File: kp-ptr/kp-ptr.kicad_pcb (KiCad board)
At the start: 2 copper layers, 125 parts, among them IC1 E22-900M22S, J2 Conn_01x02, J3 Conn_01x02, J4 USB_C_Receptacle_USB2.0, J6 Conn_01x02, J7 Conn_01x02, J8 Conn_01x02, J9 Conn_01x02, Q10 NMOS_SOT23, Q11 NMOS_SOT23, Q12 PMOS_SOT23, Q13 PMOS_SOT23, Q5 NMOS_SOT23, Q6 NMOS_SOT23, Q7 NMOS_SOT23, Q8 PMOS_SOT23, Q9 PMOS_SOT23, U1 ESP32-S3FN8, U10 USBLC6-2SC6, U3 MS560702BA03-50, U4 MMC5983MA, U5 H3LIS331, U6 L96-M33, U7 LSM6DSO32, U8 SPX3819M5-L-3-3, U9 SPX3819M5-L-1-8, Y1 7M40000005-40MHz

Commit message: Small changes before sleep Signed-off-by: kretu <krecik@gmail.com>
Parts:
- added J5: Micro_SD_Card_Det, KP-PTR_lib:GCT_MEM2051-00-195-00-A, F.Cu at (222.1, 34.6)
- moved R26 101.0 mm to (152.5, 80.0), turned to -90 degrees
- moved C33 90.5 mm to (166.3, 73.9), turned to 180 degrees
- moved C31 89.4 mm to (168.2, 70.5)
- moved R25 83.0 mm to (168.4, 73.4)
- moved R27 82.7 mm to (168.4, 71.3)
- moved C32 82.6 mm to (166.3, 73.3), turned to 180 degrees
- moved R24 79.8 mm to (167.2, 72.4)
- moved R36 44.2 mm to (213.4, 38.3), turned to 180 degrees
- moved R31 40.1 mm to (221.3, 43.7)
- moved R33 31.8 mm to (222.4, 45.7), turned to 180 degrees
- moved R32 31.5 mm to (224.7, 43.7)
- moved R28 17.6 mm to (258.5, 101.3)
- moved C36 14.4 mm to (259.5, 102.6)
- moved R39 10.1 mm to (271.4, 73.8)
- moved U8 5.60 mm to (162.6, 71.4), turned to 180 degrees
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
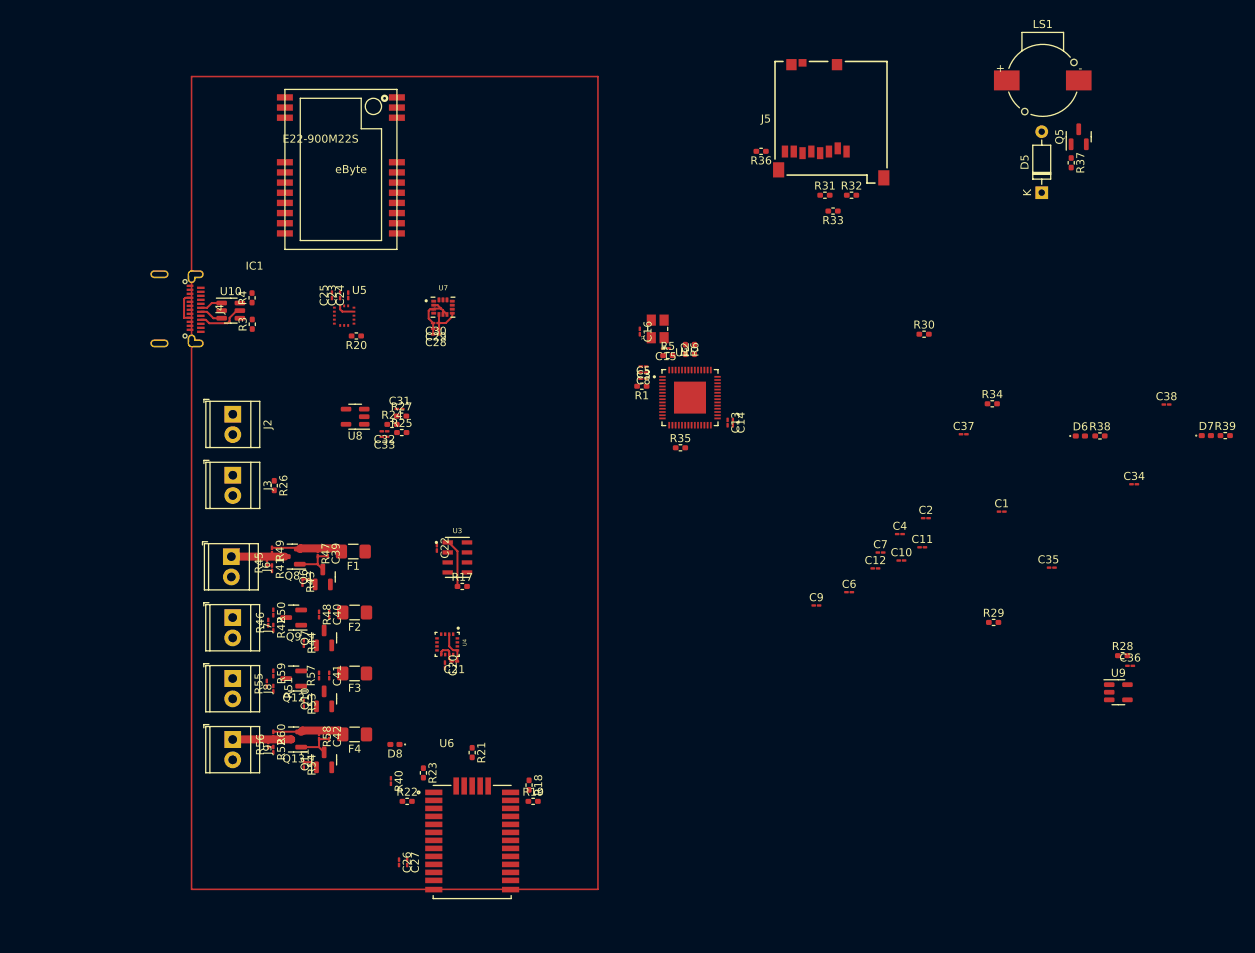
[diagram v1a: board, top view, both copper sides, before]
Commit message: Golaiath fight with board Signed-off-by: kretu <krecik@gmail.com>
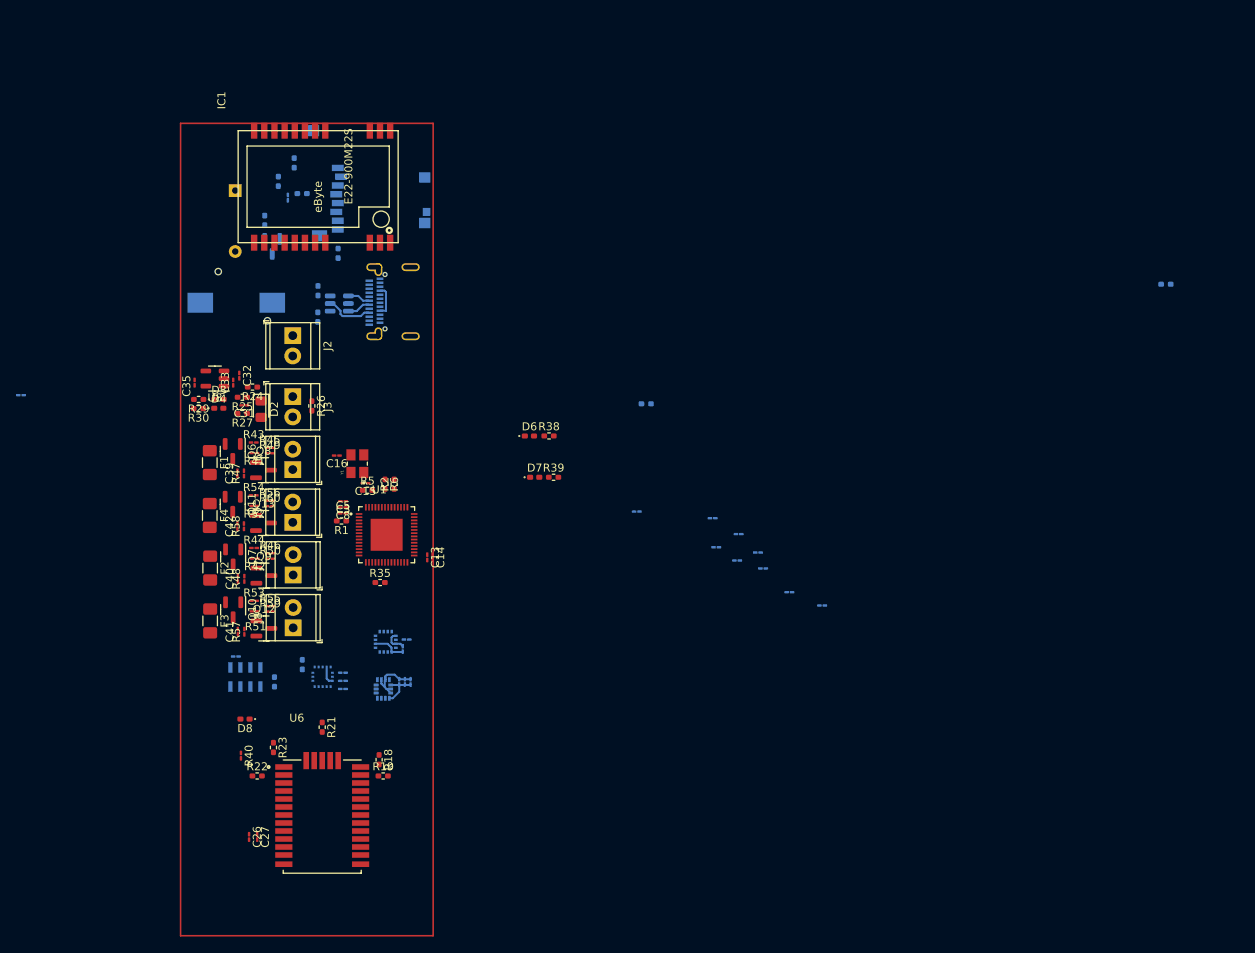
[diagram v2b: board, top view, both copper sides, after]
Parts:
- removed C34: 1uF, Capacitor_SMD:C_01005_0402Metric_Pad0.57x0.30mm_HandSolder
- removed C36: 1u, Capacitor_SMD:C_01005_0402Metric_Pad0.57x0.30mm_HandSolder
- removed U9: SPX3819M5-L-1-8, Package_TO_SOT_SMD:SOT-23-5
- added D2: D_Schottky, Diode_SMD:D_0805_2012Metric_Pad1.15x1.40mm_HandSolder, F.Cu at (150.9, 70.5)
- added D3: G, LED_SMD:LED_0402_1005Metric_Pad0.77x0.64mm_HandSolder, F.Cu at (145.6, 69.3)
- added D4: G, LED_SMD:LED_0402_1005Metric_Pad0.77x0.64mm_HandSolder, F.Cu at (145.6, 70.4)
- C1, C10, C11, C12, C2, C20, C21, C22, C23, C24, C25, C28, C29, C30, C37, C38, C4, C6, C7, C9, D5, J4, J5, LS1, Q5, R17, R20, R28, R3, R31, R32, R33, R34, R36, R37, R4, U10, U3, U4, U5, U7: moved to B.Cu
- moved C38 143.2 mm to (120.8, 68.7), turned to 180 degrees
- moved C35 109.6 mm to (142.5, 67.2), turned to 90 degrees
- moved LS1 104.6 mm to (147.8, 57.2)
- moved R29 103.2 mm to (143.1, 69.3), turned to 180 degrees
- moved Q5 101.7 mm to (152.2, 50.1), turned to -90 degrees
- moved R37 101.1 mm to (151.3, 46.9), turned to 90 degrees
- moved D5 100.8 mm to (147.6, 43.2), turned to -90 degrees
- moved R30 91.2 mm to (143.0, 70.4), turned to 180 degrees
- moved C37 89.5 mm to (154.2, 44.0), turned to -90 degrees
- moved R39 84.1 mm to (187.4, 79.0)
- moved D7 84.1 mm to (185.1, 79.0)
- moved R32 69.8 mm to (155.0, 39.7), turned to 90 degrees
- moved R33 69.4 mm to (153.0, 42.0), turned to -90 degrees
- moved D6 68.9 mm to (184.4, 73.8)
- moved R38 68.9 mm to (186.8, 73.8)
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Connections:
- J2 pad 1: +BATT -> Earth
- J2 pad 2: Earth -> +BATT
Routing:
- net Net-(C42-Pad1): track 9.59 -> 0.00 mm
- net Net-(C39-Pad1): track 8.93 -> 0.00 mm
- net Net-(J9-Pad1): track 7.33 -> 0.00 mm
- net Net-(J6-Pad1): track 6.68 -> 0.00 mm
- net +3V3: track 15.2 -> 9.26 mm
- net Net-(C42-Pad2): track 5.41 -> 0.00 mm
- net Net-(C39-Pad2): track 5.41 -> 0.00 mm
- net IGN4_EN: track 1.86 -> 0.00 mm
- net IGN1_EN: track 1.86 -> 0.00 mm
- net IGN4_DET: track 0.65 -> 0.00 mm
- net IGN1_DET: track 0.64 -> 0.00 mm
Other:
- copper layers 2 -> 4

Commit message: Weryfikacja footprintow faza I Signed-off-by: kretu <krecik@gmail.com>
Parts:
- removed R21: DNP 0 dla ublox, Resistor_SMD:R_0402_1005Metric_Pad0.72x0.64mm_HandSolder
- removed R22: DNP 0 dla L96, Resistor_SMD:R_0402_1005Metric_Pad0.72x0.64mm_HandSolder
- removed R28: DNP, Resistor_SMD:R_0402_1005Metric_Pad0.72x0.64mm_HandSolder
- removed R31: 0, Resistor_SMD:R_0402_1005Metric_Pad0.72x0.64mm_HandSolder
- added ANT1: TBD, Resistor_SMD:R_0402_1005Metric_Pad0.72x0.64mm_HandSolder, F.Cu at (233.1, 55.2)
- added C17: 100nF, Capacitor_SMD:C_01005_0402Metric_Pad0.57x0.30mm_HandSolder, F.Cu at (222.6, 56.7)
- added C18: 47p, Capacitor_SMD:C_01005_0402Metric_Pad0.57x0.30mm_HandSolder, F.Cu at (222.6, 55.0)
- added C19: DNP, Capacitor_SMD:C_01005_0402Metric_Pad0.57x0.30mm_HandSolder, F.Cu at (220.4, 58.7)
- added C34: 100n, Capacitor_SMD:C_01005_0402Metric_Pad0.57x0.30mm_HandSolder, F.Cu at (219.3, 57.0)
- added C36: 100n, Capacitor_SMD:C_0402_1005Metric_Pad0.74x0.62mm_HandSolder, F.Cu at (236.1, 57.2)
- added D9: LED, LED_SMD:LED_0402_1005Metric_Pad0.77x0.64mm_HandSolder, F.Cu at (229.8, 55.2)
- added FB1: TBD, Resistor_SMD:R_0402_1005Metric_Pad0.72x0.64mm_HandSolder, F.Cu at (229.6, 57.2)
- added R10: 2k, Resistor_SMD:R_0402_1005Metric_Pad0.72x0.64mm_HandSolder, F.Cu at (232.9, 59.2)
- added R11: 10k, Resistor_SMD:R_0402_1005Metric_Pad0.72x0.64mm_HandSolder, F.Cu at (232.9, 57.2)
- added R12: DNP, Resistor_SMD:R_0402_1005Metric_Pad0.72x0.64mm_HandSolder, F.Cu at (229.6, 59.2)
- added R13: 0R, Resistor_SMD:R_0402_1005Metric_Pad0.72x0.64mm_HandSolder, F.Cu at (236.3, 55.2)
- added R7: 10k, Resistor_SMD:R_0402_1005Metric_Pad0.72x0.64mm_HandSolder, F.Cu at (217.5, 59.4)
- added R8: 10R, Resistor_SMD:R_0402_1005Metric_Pad0.72x0.64mm_HandSolder, F.Cu at (214.3, 59.4)
- added R9: 10k, Resistor_SMD:R_0402_1005Metric_Pad0.72x0.64mm_HandSolder, F.Cu at (219.7, 55.2)
- added U9: NJG1156PCD, KP-PTR_lib:SON50P260X260X55-11N, F.Cu at (213.8, 54.5)
- C38: value ??? -> 4u7; footprint Capacitor_SMD:C_01005_0402Metric_Pad0.57x0.30mm_HandSolder -> Capacitor_SMD:C_0805_2012Metric_Pad1.18x1.45mm_HandSolder
- R23: value DNP 0 dla ublox -> DNP
- R32, R33, R34, R35, R36: value 50k -> 100k
- R37: value 220R -> 10k
- R38, R39, R40: value 220R -> 1k
- U6: value L96-M33 -> L76-L; footprint KP-PTR_lib:XCVR_L96-M33 -> KP-PTR_lib:XCVR_L76-L
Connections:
- C37 pad 1: +3V3 -> Net-(C37-Pad1)
- IC1 pad 14: unconnected-(IC1-Pad14) -> RF_BUSY
- IC1 pad 15: unconnected-(IC1-Pad15) -> RF_RST
- IC1 pad 21: unconnected-(IC1-Pad21) -> Net-(IC1-Pad21)
- IC1 pad 6: unconnected-(IC1-Pad6) -> Net-(IC1-Pad6)
- IC1 pad 7: unconnected-(IC1-Pad7) -> Net-(IC1-Pad7)
- IC1 pad 8: unconnected-(IC1-Pad8) -> Net-(IC1-Pad7)
- J5 pad 4: Net-(J5-Pad4) -> Net-(C37-Pad1)
- Q5 pad 1: Net-(Q5-Pad1) -> BUZZER
- R18 pad 1: Earth -> +3V3
- R19 pad 1: Net-(R19-Pad1) -> unconnected-(R19-Pad1)
- R37 pad 1: Net-(Q5-Pad1) -> Earth
- U6 pad 1: Net-(R23-Pad2) -> Earth
- U6 pad 11: Earth -> unconnected-(U6-Pad11)
- U6 pad 13: Earth -> Net-(U9-Pad2)
- U6 pad 14: Earth -> unconnected-(U6-Pad14)
- U6 pad 15: Earth -> unconnected-(U6-Pad15)
- U6 pad 18: Earth -> unconnected-(U6-Pad18)
- U6 pad 2: Net-(R22-Pad2) -> unconnected-(U6-Pad2)
- U6 pad 4: Earth -> unconnected-(U6-Pad4)
- U6 pad 5: Earth -> unconnected-(U6-Pad5)
- U6 pad 8: +3V3 -> Net-(R23-Pad2)
- U6 pad 9: +3V3 -> unconnected-(U6-Pad9)

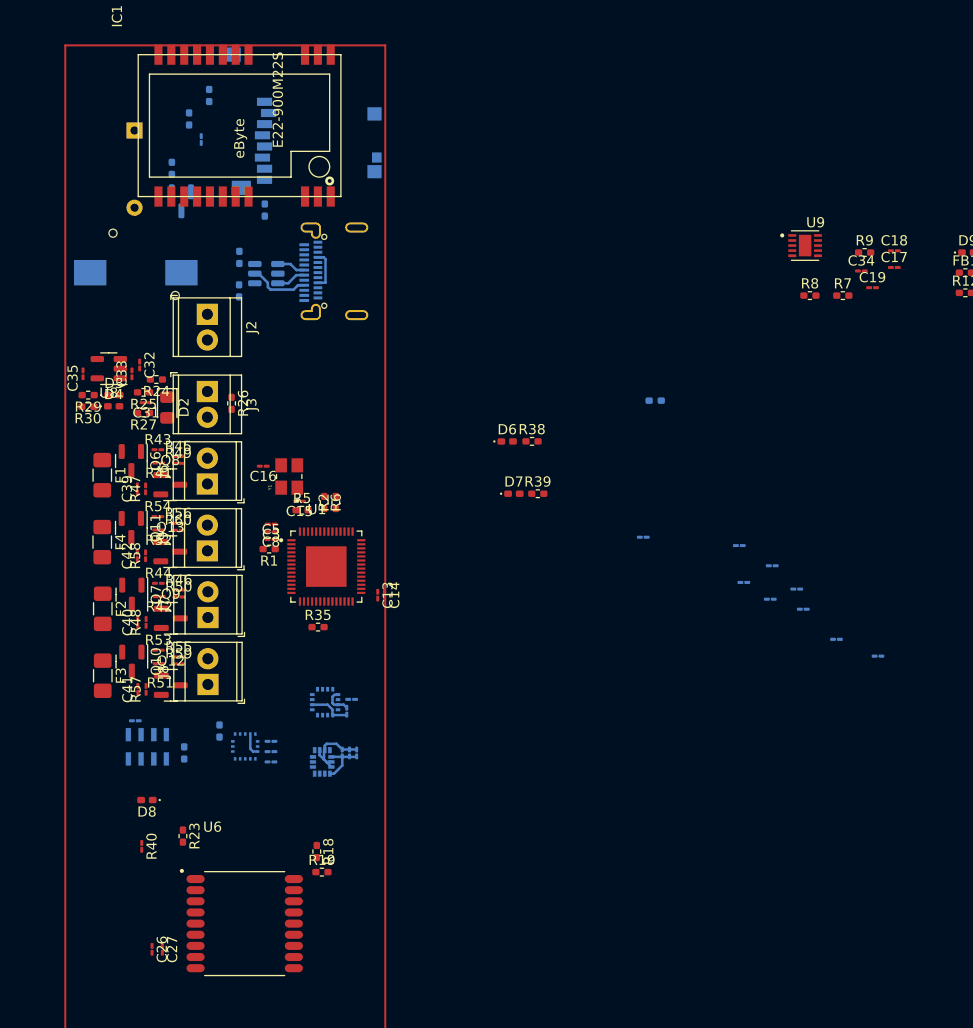
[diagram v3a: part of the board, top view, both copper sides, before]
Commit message: Footprinty drobnicy
Signed-off-by: kretu <krecik@gmail.com>
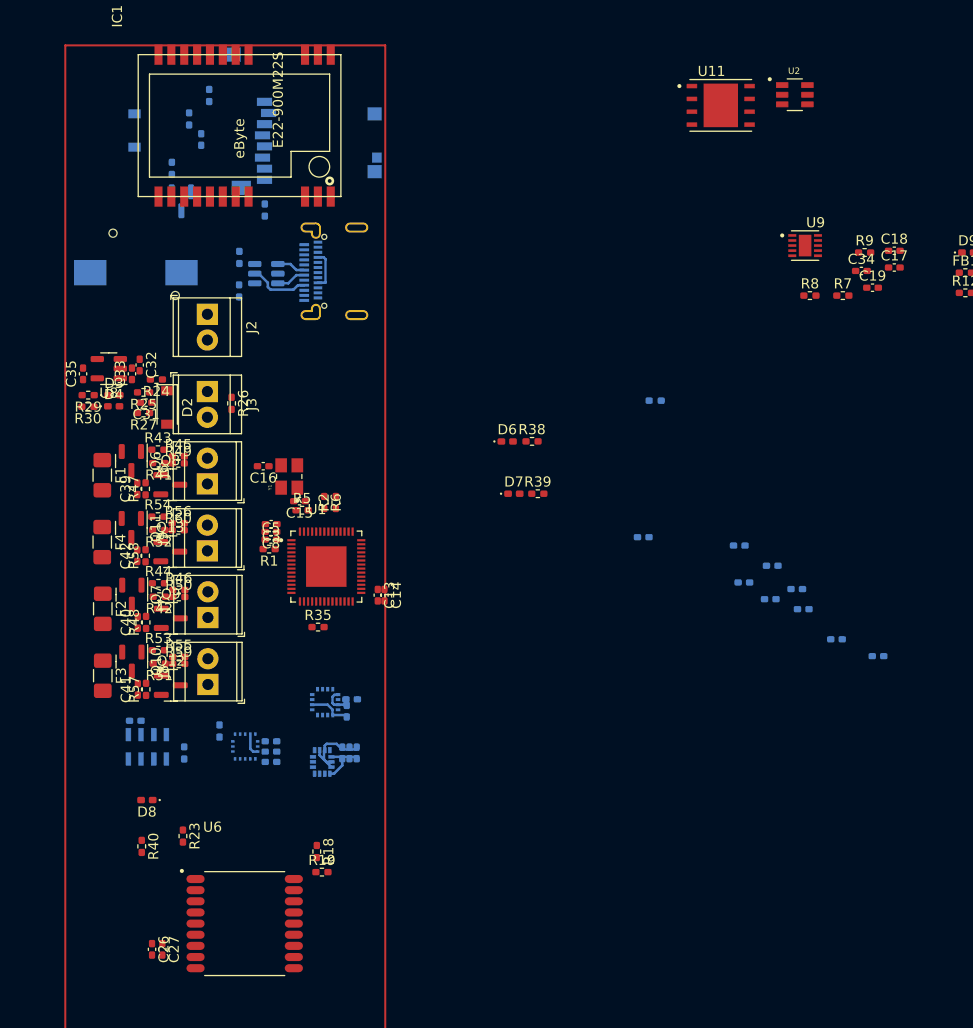
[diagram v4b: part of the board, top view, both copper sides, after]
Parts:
- added U11: W25Q128JVS, KP-PTR_lib:SON127P500X600X80-9N, F.Cu at (205.5, 40.7)
- added U2: NL27WZU04DBVT1G, KP-PTR_lib:SOT95P275X110-6N, F.Cu at (212.8, 39.6)
- C1, C10, C11, C12, C13, C14, C15, C16, C17, C18, C19, C2, C20, C21, C22, C23, C24, C25, C26, C27, C28, C29, C3, C30, C31, C32, C33, C34, C35, C37, C39, C4, C40, C41, C42, C5, C6, C7, C8, C9: footprint Capacitor_SMD:C_01005_0402Metric_Pad0.57x0.30mm_HandSolder -> Capacitor_SMD:C_0402_1005Metric_Pad0.74x0.62mm_HandSolder
- D2: footprint Diode_SMD:D_0805_2012Metric_Pad1.15x1.40mm_HandSolder -> Diode_SMD:D_SOD-123
- D5: footprint Diode_THT:D_DO-35_SOD27_P7.62mm_Horizontal -> Diode_SMD:D_SOD-123
- R40, R41, R42, R43, R44, R45, R46, R47, R48, R49, R50, R51, R52, R53, R54, R55, R56, R57, R58, R59, R60: footprint Resistor_SMD:R_01005_0402Metric_Pad0.57x0.30mm_HandSolder -> Resistor_SMD:R_0402_1005Metric_Pad0.72x0.64mm_HandSolder

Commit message: Update po spotkaniu
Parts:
- added ANT2: PCB_antenna, RF_Antenna:Texas_SWRA117D_2.4GHz_Right, F.Cu at (96.5, 71.1)
- added ANT3: APAE1575R1340ABDD6-T, KP-PTR_lib:APAE1575 13x13x4mm GPS Patch Antenna, F.Cu at (119.9, 105.5)
- added C1: 56pF, Capacitor_SMD:C_0402_1005Metric, F.Cu at (121.8, 94.1)
- added C18: 1nF, Capacitor_SMD:C_0402_1005Metric, F.Cu at (119.8, 91.2)
- added C19: DNP, Capacitor_SMD:C_0402_1005Metric, F.Cu at (123.8, 97.0)
- added C34: DNP, Capacitor_SMD:C_0402_1005Metric, F.Cu at (117.8, 90.0)
- added C43: TBD, Capacitor_SMD:C_0402_1005Metric, F.Cu at (115.8, 90.0)
- added C44: 1uF, Capacitor_SMD:C_0402_1005Metric, F.Cu at (122.1, 80.8)
- added C45: 10u, Capacitor_SMD:C_0402_1005Metric, F.Cu at (117.2, 76.4)
- added C46: 1uF, Capacitor_SMD:C_0402_1005Metric, F.Cu at (109.2, 55.4)
- added C47: 100n, Capacitor_SMD:C_0402_1005Metric, F.Cu at (111.1, 55.0)
- added C48: 100nF, Capacitor_SMD:C_0402_1005Metric, F.Cu at (93.3, 80.1)
- added C49: 100nF, Capacitor_SMD:C_0402_1005Metric, F.Cu at (107.5, 98.3)
- added C50: 100nF, Capacitor_SMD:C_0402_1005Metric, F.Cu at (99.0, 90.5)
- added D1: BLUE, LED_SMD:LED_0603_1608Metric, F.Cu at (117.5, 96.4)
- added D10: TBD, Diode_SMD:D_SOD-123, F.Cu at (113.4, 59.3)
- added D11: G, LED_SMD:LED_0603_1608Metric, F.Cu at (114.1, 74.4)
- added D12: LED, LED_SMD:LED_0603_1608Metric, F.Cu at (106.9, 110.5)
- added D6: TBD, Diode_SMD:D_SOD-123, F.Cu at (114.5, 95.6)
- added D8: D_Schottky, Diode_SMD:D_SOD-123, F.Cu at (114.5, 79.3)
- added F6: 500mA, Fuse:Fuse_0805_2012Metric, F.Cu at (117.7, 80.0)
- added FB1: 200mA, Resistor_SMD:R_0402_1005Metric, F.Cu at (119.8, 97.0)
- added FB2: 1000mA, Resistor_SMD:R_0603_1608Metric, F.Cu at (106.9, 54.9)
- added J1: ESP32_PROG_CON, Connector_PinHeader_1.27mm:PinHeader_1x06_P1.27mm_Vertical, F.Cu at (92.0, 56.2)
- added J10: Conn_01x10_Male, Connector_JST:JST_GH_BM10B-GHS-TBT_1x10-1MP_P1.25mm_Vertical, F.Cu at (94.2, 103.5)
- added J11: u.fl, Connector_Coaxial:U.FL_Hirose_U.FL-R-SMT-1_Vertical, F.Cu at (108.7, 59.7)
- added J12: Conn_01x06_Male, Connector_JST:JST_GH_BM06B-GHS-TBT_1x06-1MP_P1.25mm_Vertical, F.Cu at (101.8, 106.0)
- added J13: Conn_01x02_Male, TerminalBlock_TE-Connectivity:TerminalBlock_TE_282834-2_1x02_P2.54mm_Horizontal, F.Cu at (102.3, 97.0)
- added J5: Conn_01x06_Male, Connector_JST:JST_GH_BM06B-GHS-TBT_1x06-1MP_P1.25mm_Vertical, F.Cu at (94.2, 88.0)
- added L2: 1.8nH, Inductor_SMD:L_0402_1005Metric, F.Cu at (98.4, 64.7)
- added L3: 2nH, Inductor_SMD:L_0402_1005Metric, F.Cu at (101.0, 73.4)
- added L5: 10nH, Inductor_SMD:L_0402_1005Metric, F.Cu at (117.2, 92.9)
- added R14: 1k, Resistor_SMD:R_0402_1005Metric, F.Cu at (98.4, 67.6)
- added R15: 1k, Resistor_SMD:R_0402_1005Metric, F.Cu at (121.8, 97.0)
- added R16: 4k7, Resistor_SMD:R_0402_1005Metric, F.Cu at (119.8, 94.1)
- added R21: 10k, Resistor_SMD:R_0402_1005Metric, F.Cu at (113.8, 88.3)
- added R22: 100R, Resistor_SMD:R_0402_1005Metric, F.Cu at (113.8, 91.2)
- added R23: 10k, Resistor_SMD:R_0402_1005Metric, F.Cu at (120.1, 80.8)
- added R28: 10k, Resistor_SMD:R_0402_1005Metric, F.Cu at (106.7, 51.4)
- added R31: DNP, Resistor_SMD:R_0402_1005Metric, F.Cu at (116.0, 60.8)
- added R34: 1k, Resistor_SMD:R_0402_1005Metric, F.Cu at (106.6, 101.2)
- added R35: 1k, Resistor_SMD:R_0402_1005Metric, F.Cu at (106.6, 107.0)
- added R36: 1k, Resistor_SMD:R_0402_1005Metric, F.Cu at (108.6, 107.0)
- added R40: 1k, Resistor_SMD:R_0402_1005Metric, F.Cu at (91.3, 80.1)
- added R6: 1k, Resistor_SMD:R_0402_1005Metric, F.Cu at (98.4, 73.4)
- added R61: 1k, Resistor_SMD:R_0402_1005Metric, F.Cu at (106.6, 104.1)
- added R62: 1k, Resistor_SMD:R_0402_1005Metric, F.Cu at (108.6, 101.2)
- added R63: 10k, Resistor_SMD:R_0402_1005Metric, F.Cu at (108.6, 104.1)
- added R8: 1k, Resistor_SMD:R_0402_1005Metric, F.Cu at (98.4, 70.5)
- C10, C11, C12, C13, C14, C15, C16, C17, C20, C21, C22, C23, C24, C25, C26, C27, C28, C29, C30, C32, C33, C35, C36, C37, C39, C4, C40, C41, C42, C5, C6, C7: footprint Capacitor_SMD:C_0402_1005Metric_Pad0.74x0.62mm_HandSolder -> Capacitor_SMD:C_0402_1005Metric
- C2: value TBD -> 4pF; footprint Capacitor_SMD:C_0402_1005Metric_Pad0.74x0.62mm_HandSolder -> Capacitor_SMD:C_0402_1005Metric
- C3: value TBD -> 5pF; footprint Capacitor_SMD:C_0402_1005Metric_Pad0.74x0.62mm_HandSolder -> Capacitor_SMD:C_0402_1005Metric
- C31: value 1uF -> 10n; footprint Capacitor_SMD:C_0402_1005Metric_Pad0.74x0.62mm_HandSolder -> Capacitor_SMD:C_0402_1005Metric
- C38: footprint Capacitor_SMD:C_0805_2012Metric_Pad1.18x1.45mm_HandSolder -> Capacitor_SMD:C_0402_1005Metric
- C8: value TBD -> 100n; footprint Capacitor_SMD:C_0402_1005Metric_Pad0.74x0.62mm_HandSolder -> Capacitor_SMD:C_0402_1005Metric
- C9: value 10u -> 10n; footprint Capacitor_SMD:C_0402_1005Metric_Pad0.74x0.62mm_HandSolder -> Capacitor_SMD:C_0402_1005Metric
- D3, D4, D7, D9: footprint LED_SMD:LED_0402_1005Metric_Pad0.77x0.64mm_HandSolder -> LED_SMD:LED_0603_1608Metric
- F1, F2, F3, F4: footprint Fuse:Fuse_1206_3216Metric_Pad1.42x1.75mm_HandSolder -> Fuse:Fuse_0805_2012Metric
- J4: footprint KP-PTR_lib:217B-BC02 -> Connector_USB:USB_C_Receptacle_GCT_USB4085
- LS1: footprint KP-PTR_lib:BUZZER CBT-09 -> Buzzer_Beeper:Buzzer_12x9.5RM7.6
- R1, R11, R12, R13, R17, R18, R19, R2, R20, R24, R25, R26, R27, R29, R3, R30, R32, R33, R37, R38, R39, R4, R41, R42, R43, R44, R45, R46, R47, R48, R49, R5, R50, R51, R52, R53, R54, R55, R56, R57, R58, R59, R60, R7, R9: footprint Resistor_SMD:R_0402_1005Metric_Pad0.72x0.64mm_HandSolder -> Resistor_SMD:R_0402_1005Metric
- R10: value 2k -> 2k2; footprint Resistor_SMD:R_0402_1005Metric_Pad0.72x0.64mm_HandSolder -> Resistor_SMD:R_0402_1005Metric
- moved C12 1.08 mm to (213.4, 91.4)
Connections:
- net VDD_SPI renamed Net-(C13-Pad1)
- C26 pad 1: +3V3 -> +3.3VADC
- C27 pad 1: +3V3 -> +3.3VADC
- C36 pad 1: +3V3 -> +3.3VP
- C37 pad 1: Net-(C37-Pad1) -> +3V3
- C38 pad 1: +3V3 -> +3.3VP
- IC1 pad 9: +3V3 -> +3.3VP
- R10 pad 1: +3V3 -> +3.3VP
- R11 pad 1: +3V3 -> +3.3VP
- R18 pad 2: U0TXD -> GPS_IN
- R19 pad 1: unconnected-(R19-Pad1) -> Net-(R19-Pad1)
- R19 pad 2: U0RXD -> GPS_OUT
- R2 pad 1: Net-(R2-Pad1) -> BOOT_PIN
- R2 pad 2: U0TXD -> Net-(R2-Pad2)
- R24 pad 1: VDD -> VCC
- R32 pad 1: Net-(J5-Pad1) -> +3V3
- R32 pad 2: +3V3 -> SPI_CS_FLASH
- R33 pad 1: SPI_CS_SDCARD -> +3V3
- R33 pad 2: +3V3 -> SPI_CLK
- R38 pad 1: Net-(D6-Pad2) -> Net-(R38-Pad1)
- U1 pad 48: unconnected-(U1-Pad48) -> GPIO42
- U1 pad 49: Net-(R2-Pad1) -> U0TXD
- U1 pad 51: Net-(R6-Pad2) -> BUZZER
- U1 pad 52: GPIO46 -> LED2
- U1 pad 8: GPIO3 -> RF_RST
- U11 pad 1: unconnected-(U11-Pad1) -> SPI_CS_FLASH
- U11 pad 2: unconnected-(U11-Pad2) -> SPI_MISO
- U11 pad 3: unconnected-(U11-Pad3) -> +3V3
- U11 pad 4: unconnected-(U11-Pad4) -> Earth
- U11 pad 5: unconnected-(U11-Pad5) -> SPI_MOSI
- U11 pad 6: unconnected-(U11-Pad6) -> SPI_CLK
- U11 pad 7: unconnected-(U11-Pad7) -> +3V3
- U11 pad 8: unconnected-(U11-Pad8) -> +3V3
- U2 pad 5: +3V3 -> +3.3VP
- U6 pad 11: unconnected-(U6-Pad11) -> Net-(U6-Pad11)
- U6 pad 13: Net-(U6-Pad13) -> ANTON
- U6 pad 2: unconnected-(U6-Pad2) -> Net-(R19-Pad1)
- U6 pad 3: unconnected-(U6-Pad3) -> Net-(U6-Pad3)
- U6 pad 4: unconnected-(U6-Pad4) -> Net-(U6-Pad4)
- U6 pad 6: unconnected-(U6-Pad6) -> +3.3VADC
- U6 pad 8: Net-(R23-Pad2) -> +3.3VADC
- U9 pad 1: unconnected-(U9-Pad1) -> Earth
- U9 pad 10: unconnected-(U9-Pad10) -> Net-(U9-Pad10)
- U9 pad 2: Net-(U6-Pad13) -> Net-(U9-Pad2)
- U9 pad 3: unconnected-(U9-Pad3) -> +3.3VADC
- U9 pad 4: unconnected-(U9-Pad4) -> Earth
- U9 pad 5: unconnected-(U9-Pad5) -> Net-(U9-Pad5)
- U9 pad 6: Earth -> (no net)
- U9 pad 9: unconnected-(U9-Pad9) -> Earth
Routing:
- net unconnected-(J4-PadA5): track 0.00 -> 5.95 mm
- net Net-(J4-PadA7): track 2.94 -> 0.00 mm
- net Net-(J4-PadA6): track 2.85 -> 0.00 mm
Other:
- board outline added: 31.6 x 101.5 mm
